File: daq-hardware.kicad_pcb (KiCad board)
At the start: 2 copper layers, 100 x 60 mm, 35 parts, among them J1 USB_B, J2 Micro_SD_Card_Det_Hirose_DM3AT, J3 Screw_Terminal_Thermo_1, J4 Screw_Terminal_Thermo_2, J5 Screw_Terminal_Thermo_3, J6 Screw_Terminal_Thermo_4, J7 Conn_01x02, J8 Screw_Terminal_01x02, Q1 MMDT2222A, U1 CP2102N-A01-GQFN24, U2 ESP32-WROOM-32D, U4 MAX31855RASA, U5 MAX31855RASA, U6 MAX31855RASA, U7 MAX31855RASA, U8 TPS62160DGK

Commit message: Layout for Pyros
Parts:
- added D3: FIRING, LED_SMD:LED_0805_2012Metric, F.Cu at (271.5, 80.0)
- added D4: DIODE, Diode_SMD:D_SMA, F.Cu at (272.8, 85.6)
- added J10: Screw_Terminal_01x02, TerminalBlock_Phoenix:TerminalBlock_Phoenix_MPT-0,5-2-2.54_1x02_P2.54mm_Horizontal, F.Cu at (280.9, 80.8)
- added J11: Screw_Terminal_01x02, TerminalBlock_Phoenix:TerminalBlock_Phoenix_MPT-0,5-2-2.54_1x02_P2.54mm_Horizontal, F.Cu at (280.9, 88.1)
- added JP1: SolderJumper_3_Open, Jumper:SolderJumper-3_P2.0mm_Open_TrianglePad1.0x1.5mm, F.Cu at (263.4, 75.2)
- added Q2: PMV20ENR, Package_TO_SOT_SMD:SOT-23, F.Cu at (267.2, 87.6)
- added R23: 1k, Resistor_SMD:R_0603_1608Metric, F.Cu at (273.8, 80.3)
- added R24: 500, Resistor_SMD:R_0603_1608Metric, F.Cu at (260.4, 87.6)
- added R25: 500, Resistor_SMD:R_0603_1608Metric, F.Cu at (263.1, 87.6)
- added U10: LTV-817S, Package_DIP:SMDIP-4_W9.53mm, F.Cu at (264.2, 82.0)
- renumbered C5 to C10, C6 to C11, C7 to C12, C8 to C13, C9 to C14, C10 to C15, C11 to C16, C14 to C6, C15 to C7, C4 to C9, J7 to J3, J8 to J4, J3 to J6, J4 to J7, J5 to J8, J6 to J9, R16 to R18, R17 to R19, R18 to R20, R3 to R4, R4 to R5, U8 to U4, U4 to U6, U5 to U7, U6 to U8, U7 to U9
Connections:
- J2 pad 10: (no net) -> Net-(J2-Pad10)
- J2 pad 9: (no net) -> Net-(J2-Pad9)
- U1 pad 1: (no net) -> Net-(U1-Pad1)
- U1 pad 10: (no net) -> Net-(U1-Pad10)
- U1 pad 11: (no net) -> Net-(U1-Pad11)
- U1 pad 12: (no net) -> Net-(U1-Pad12)
- U1 pad 13: (no net) -> Net-(U1-Pad13)
- U1 pad 14: (no net) -> Net-(U1-Pad14)
- U1 pad 15: (no net) -> Net-(U1-Pad15)
- U1 pad 16: (no net) -> Net-(U1-Pad16)
- U1 pad 17: (no net) -> Net-(U1-Pad17)
- U1 pad 18: (no net) -> Net-(U1-Pad18)
- U1 pad 19: (no net) -> Net-(U1-Pad19)
- U1 pad 22: (no net) -> Net-(U1-Pad22)
- U1 pad 23: (no net) -> Net-(U1-Pad23)
- U1 pad 24: (no net) -> Net-(U1-Pad24)
- U1 pad 8: (no net) -> Net-(R2-Pad2)
- U1 pad 9: (no net) -> Net-(U1-Pad9)
- U2 pad 17: (no net) -> Net-(U2-Pad17)
- U2 pad 18: (no net) -> Net-(U2-Pad18)
- U2 pad 19: (no net) -> Net-(U2-Pad19)
- U2 pad 20: (no net) -> Net-(U2-Pad20)
- U2 pad 21: (no net) -> Net-(U2-Pad21)
- U2 pad 22: (no net) -> Net-(U2-Pad22)
- U2 pad 27: (no net) -> Net-(U2-Pad27)
- U2 pad 28: (no net) -> Net-(U2-Pad28)
- U2 pad 29: (no net) -> /LED
- U2 pad 32: (no net) -> Net-(U2-Pad32)
- U2 pad 33: (no net) -> /SDA
- U2 pad 36: (no net) -> /SCL
- U2 pad 4: (no net) -> Net-(U2-Pad4)
- U2 pad 5: (no net) -> Net-(U2-Pad5)
- U2 pad 6: (no net) -> /PTAP1
- U2 pad 7: (no net) -> /PTAP3
- U2 pad 9: (no net) -> /PTAP2
- U4 pad 7: (no net) -> Net-(L1-Pad1)
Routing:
- net GND: track 0.00 -> 35.4 mm
- net Net-(D3-Pad2): track 0.00 -> 27.0 mm
- net Net-(J10-Pad1): track 0.00 -> 17.8 mm
- net Net-(D4-Pad2): track 0.00 -> 17.7 mm
- net Net-(D4-Pad1): track 0.00 -> 14.2 mm, vias 0 -> 1
- net Net-(R25-Pad1): track 0.00 -> 7.31 mm
- net +3V3: track 0.00 -> 6.53 mm
- net /pyro/CONT: track 0.00 -> 3.93 mm
- net Net-(D3-Pad1): track 0.00 -> 2.33 mm
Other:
- copper layers 2 -> 4
- net class Default: clearance 0.2 -> 0.127; trace_width 0.25 -> 0.2; via_dia 0.8 -> 0.6; via_drill 0.4 -> 0.35
- rule trace_clearance: 0.2 -> 0.127

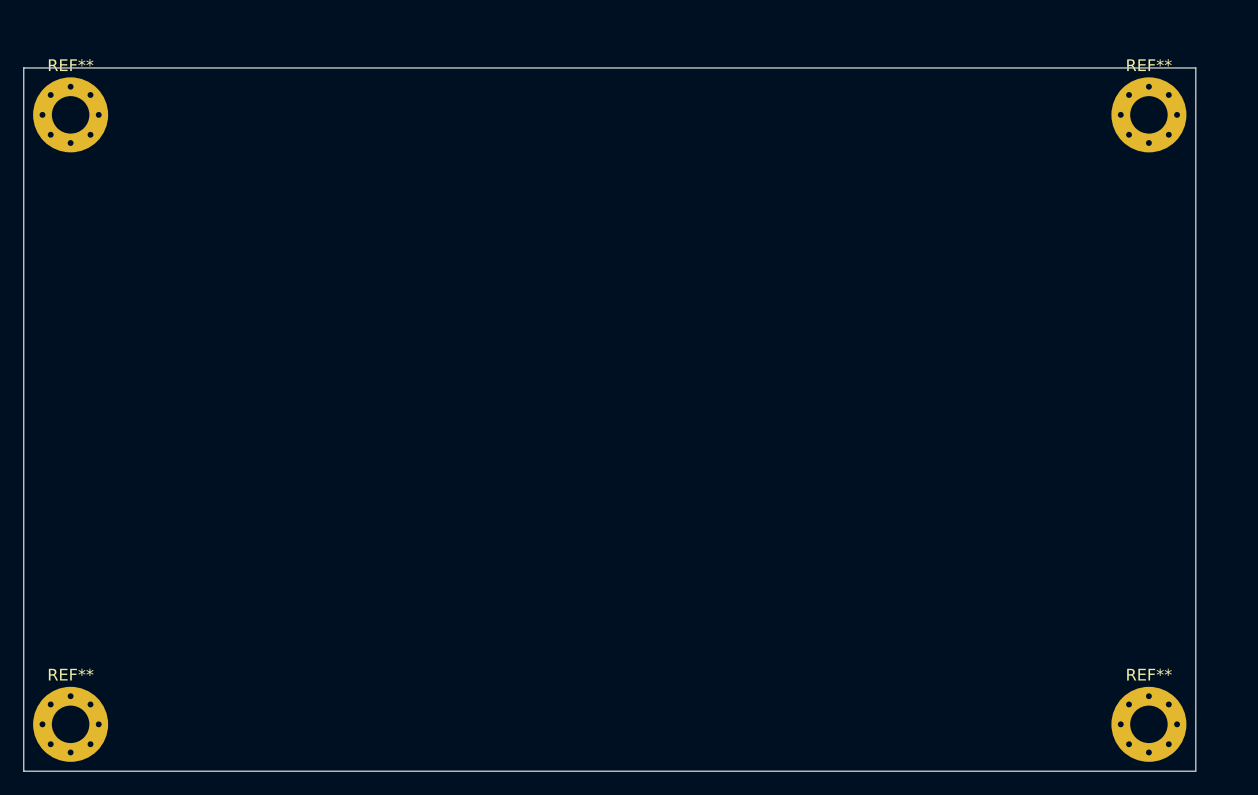
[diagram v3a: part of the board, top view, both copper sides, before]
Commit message: Via Shielding
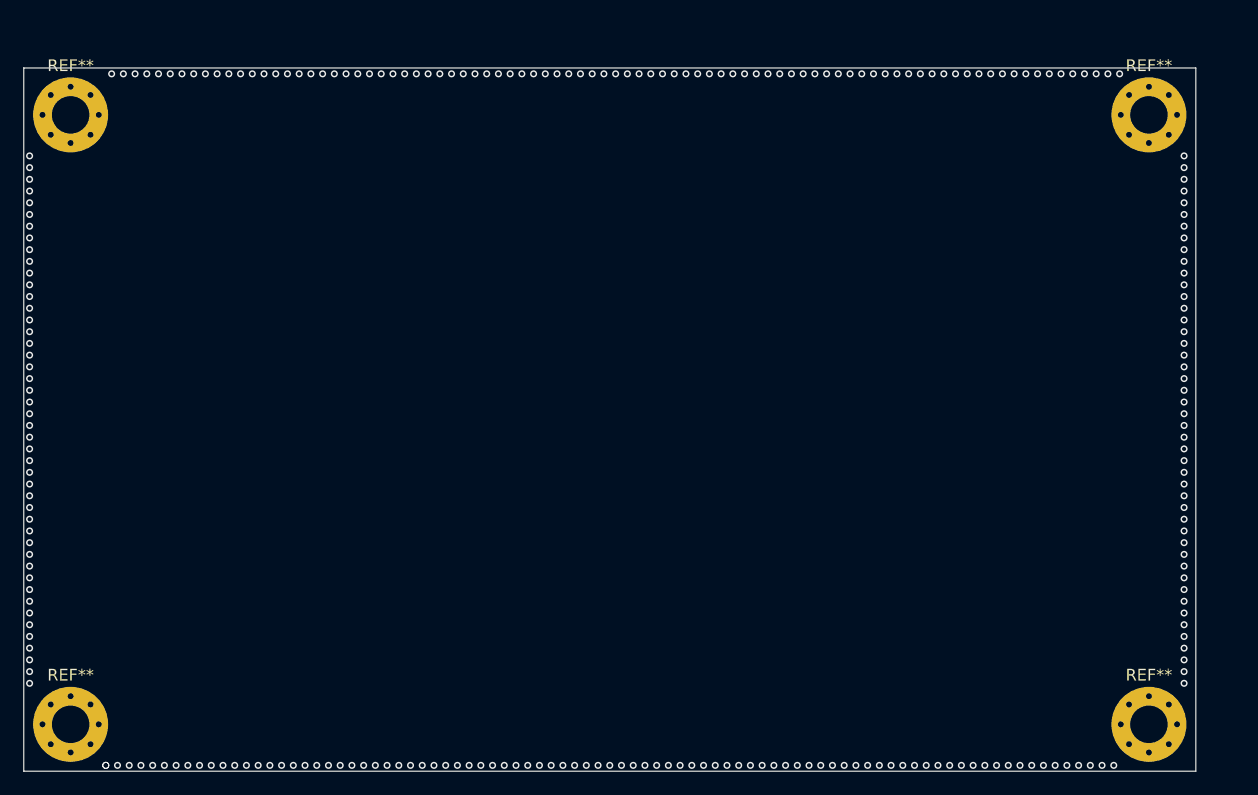
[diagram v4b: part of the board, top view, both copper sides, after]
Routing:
- net GND: vias 0 -> 266
- net (no net): vias 0 -> 1
- added copper zone on In1.Cu, net GND

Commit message: Not sure if this is gonna overwrite stuff but I try to push this anyway
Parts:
- moved JP1 105.1 mm to (169.4, 122.2)
- moved Q2 105.1 mm to (173.2, 134.6)
- moved R24 105.1 mm to (166.3, 134.6)
- moved U10 105.1 mm to (170.2, 129.0)
- moved D3 105.1 mm to (177.5, 127.0)
- moved D4 105.1 mm to (178.8, 132.6)
- moved R23 105.1 mm to (179.8, 127.3)
- moved R25 105.1 mm to (169.1, 134.6)
- moved J10 105.1 mm to (186.9, 127.8)
- moved J11 105.1 mm to (186.9, 135.1)
- moved C9 99.9 mm to (182.2, 91.5), turned to 180 degrees
- moved U9 96.9 mm to (180.0, 95.4), turned to 180 degrees
- moved U2 94.7 mm to (110.0, 120.5)
- moved C16 93.9 mm to (186.0, 94.2), turned to 270 degrees
- moved C15 90.3 mm to (182.2, 99.5), turned to 180 degrees
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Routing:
- net /SCLK: track 0.00 -> 96.6 mm
- net /MISO: track 0.00 -> 93.2 mm, vias 0 -> 2
- net /~TC_CS4: track 0.00 -> 87.1 mm, vias 0 -> 2
- net /~TC_CS2: track 0.00 -> 78.4 mm, vias 0 -> 2
- net /~TC_CS1: track 0.00 -> 73.7 mm, vias 0 -> 2
- net /~TC_CS3: track 0.00 -> 72.6 mm
- net VDD: track 0.00 -> 58.1 mm, vias 0 -> 2
- net GND: track 35.4 -> 75.4 mm, vias 266 -> 283
- net /SD_CLK: track 0.00 -> 36.9 mm, vias 0 -> 1
- net /SD_D1: track 0.00 -> 35.7 mm, vias 0 -> 1
- net +3V3: track 6.53 -> 40.3 mm, vias 0 -> 10
- net /RESET: track 0.00 -> 33.2 mm, vias 0 -> 2
- net /SD_D0: track 0.00 -> 26.0 mm, vias 0 -> 1
- net Net-(J1-Pad3): track 0.00 -> 23.6 mm
- net /SD_CMD: track 0.00 -> 21.1 mm, vias 0 -> 1
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
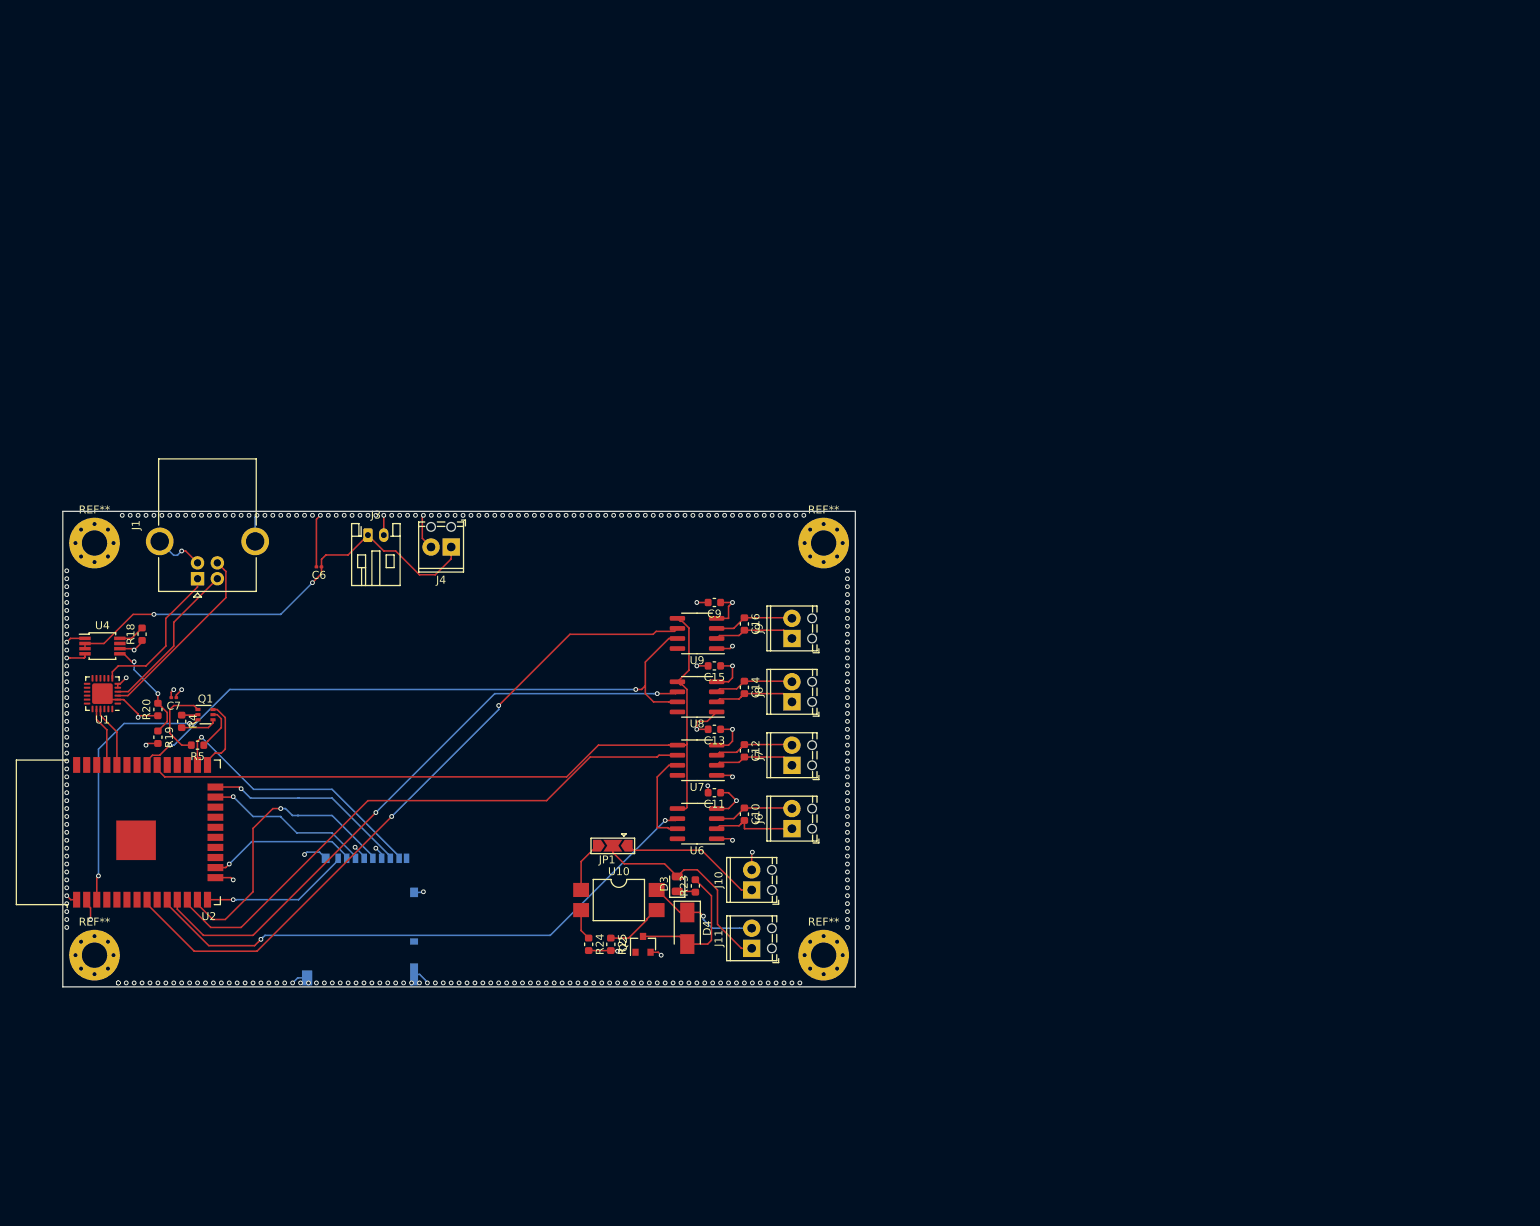
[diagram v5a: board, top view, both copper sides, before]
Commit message: Fixed conflicts, assigned all footprints.
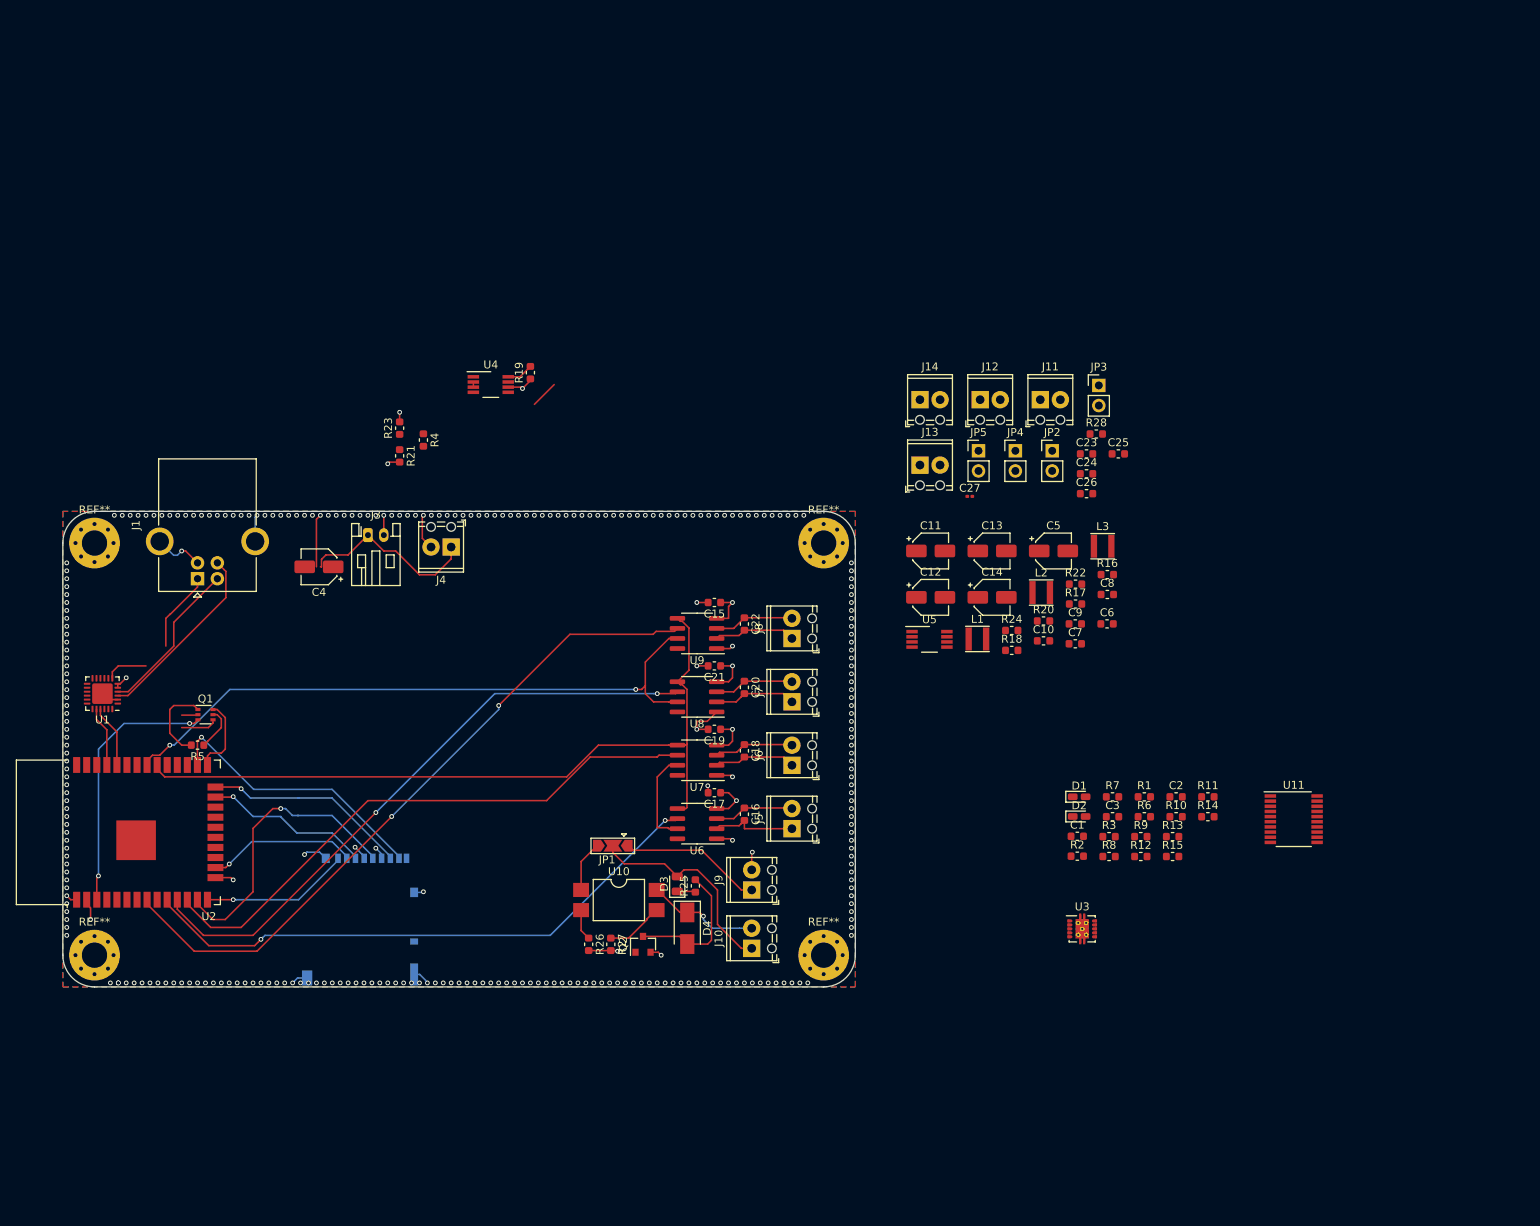
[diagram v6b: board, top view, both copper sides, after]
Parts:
- added C1: 100n, Capacitor_SMD:C_0603_1608Metric, F.Cu at (228.0, 121.0)
- added C10: 100n, Capacitor_SMD:C_0603_1608Metric, F.Cu at (223.7, 96.3)
- added C11: 10u, Capacitor_SMD:CP_Elec_4x5.4, F.Cu at (209.5, 85.0)
- added C12: 10u, Capacitor_SMD:CP_Elec_4x5.4, F.Cu at (209.5, 90.8)
- added C13: 10u, Capacitor_SMD:CP_Elec_4x5.4, F.Cu at (217.2, 85.0)
- added C14: 10u, Capacitor_SMD:CP_Elec_4x5.4, F.Cu at (217.2, 90.8)
- added C2: 1nF, Capacitor_SMD:C_0603_1608Metric, F.Cu at (240.5, 116.0)
- added C23: 10nF, Capacitor_SMD:C_0603_1608Metric, F.Cu at (229.2, 72.8)
- added C24: 10nF, Capacitor_SMD:C_0603_1608Metric, F.Cu at (229.2, 75.3)
- added C25: 10nF, Capacitor_SMD:C_0603_1608Metric, F.Cu at (233.2, 72.8)
- added C26: 10nF, Capacitor_SMD:C_0603_1608Metric, F.Cu at (229.2, 77.8)
- added C27: 220nF, Capacitor_SMD:C_0201_0603Metric, F.Cu at (214.4, 78.1)
- added C3: 1nF, Capacitor_SMD:C_0603_1608Metric, F.Cu at (232.4, 118.5)
- added C5: 10u, Capacitor_SMD:CP_Elec_4x5.4, F.Cu at (225.0, 85.0)
- added C6: 4u7, Capacitor_SMD:C_0603_1608Metric, F.Cu at (231.8, 94.2)
- added C8: 1u, Capacitor_SMD:C_0603_1608Metric, F.Cu at (231.8, 90.5)
- added C9: 1u, Capacitor_SMD:C_0603_1608Metric, F.Cu at (227.8, 94.2)
- added D1: LED, Diode_SMD:D_0603_1608Metric_Castellated, F.Cu at (228.2, 116.0)
- added D2: LED, Diode_SMD:D_0603_1608Metric_Castellated, F.Cu at (228.2, 118.5)
- added J11: Screw_Terminal_01x01, TerminalBlock_Phoenix:TerminalBlock_Phoenix_MPT-0,5-2-2.54_1x02_P2.54mm_Horizontal, F.Cu at (223.3, 65.9)
- added J12: Screw_Terminal_01x01, TerminalBlock_Phoenix:TerminalBlock_Phoenix_MPT-0,5-2-2.54_1x02_P2.54mm_Horizontal, F.Cu at (215.7, 65.9)
- added J13: Screw_Terminal_01x01, TerminalBlock_Phoenix:TerminalBlock_Phoenix_MPT-0,5-2-2.54_1x02_P2.54mm_Horizontal, F.Cu at (208.2, 74.2)
- added J14: Screw_Terminal_01x01, TerminalBlock_Phoenix:TerminalBlock_Phoenix_MPT-0,5-2-2.54_1x02_P2.54mm_Horizontal, F.Cu at (208.2, 65.9)
- added JP2: Jumper, Connector_PinHeader_2.54mm:PinHeader_1x02_P2.54mm_Vertical, F.Cu at (224.8, 72.4)
- added JP3: Jumper, Connector_PinHeader_2.54mm:PinHeader_1x02_P2.54mm_Vertical, F.Cu at (230.7, 64.1)
- added JP4: Jumper, Connector_PinHeader_2.54mm:PinHeader_1x02_P2.54mm_Vertical, F.Cu at (220.2, 72.4)
- added JP5: Jumper, Connector_PinHeader_2.54mm:PinHeader_1x02_P2.54mm_Vertical, F.Cu at (215.5, 72.4)
- added L1: 10u, Inductor_SMD:L_Taiyo-Yuden_NR-30xx, F.Cu at (215.4, 96.1)
- added L2: 2u2, Inductor_SMD:L_Taiyo-Yuden_NR-30xx, F.Cu at (223.4, 90.2)
- added L3: 2u2, Inductor_SMD:L_Taiyo-Yuden_NR-30xx, F.Cu at (231.2, 84.4)
- added R1: 10k, Resistor_SMD:R_0603_1608Metric, F.Cu at (236.5, 116.0)
- added R10: 470, Resistor_SMD:R_0603_1608Metric, F.Cu at (240.5, 118.5)
- added R11: 10k, Resistor_SMD:R_0603_1608Metric, F.Cu at (244.5, 116.0)
- added R12: 10k, Resistor_SMD:R_0603_1608Metric, F.Cu at (236.0, 123.5)
- added R13: 10k, Resistor_SMD:R_0603_1608Metric, F.Cu at (240.0, 121.0)
- added R14: 10k, Resistor_SMD:R_0603_1608Metric, F.Cu at (244.5, 118.5)
- added R15: 10k, Resistor_SMD:R_0603_1608Metric, F.Cu at (240.0, 123.5)
- added R16: 230k, Resistor_SMD:R_0603_1608Metric, F.Cu at (231.8, 88.0)
- added R17: 10k, Resistor_SMD:R_0603_1608Metric, F.Cu at (227.8, 91.7)
- added R18: 200k, Resistor_SMD:R_0603_1608Metric, F.Cu at (219.7, 97.5)
- added R2: 22k1, Resistor_SMD:R_0603_1608Metric, F.Cu at (228.0, 123.5)
- added R20: 100k, Resistor_SMD:R_0603_1608Metric, F.Cu at (223.7, 93.8)
- added R22: 52k5, Resistor_SMD:R_0603_1608Metric, F.Cu at (227.8, 89.2)
- added R24: 10k, Resistor_SMD:R_0603_1608Metric, F.Cu at (219.7, 95.0)
- added R28: 10k, Resistor_SMD:R_0603_1608Metric, F.Cu at (230.4, 70.2)
- added R3: 47k5, Resistor_SMD:R_0603_1608Metric, F.Cu at (232.0, 121.0)
- added R6: 10k, Resistor_SMD:R_0603_1608Metric, F.Cu at (236.5, 118.5)
- added R7: 470, Resistor_SMD:R_0603_1608Metric, F.Cu at (232.4, 116.0)
- added R8: 470, Resistor_SMD:R_0603_1608Metric, F.Cu at (232.0, 123.5)
- added R9: 470, Resistor_SMD:R_0603_1608Metric, F.Cu at (236.0, 121.0)
- added U11: ADS131M04, Housings_SSOP:TSSOP-20_4.4x6.5mm_Pitch0.65mm, F.Cu at (255.3, 118.8)
- added U3: TPS61093, Housings_SON:Texas_S-PWSON-N10_ThermalVias, F.Cu at (228.6, 132.7)
- added U5: TPS62160DGK, Housings_SSOP:VSSOP-8_3.0x3.0mm_Pitch0.65mm, F.Cu at (209.3, 96.2)
- C4: renamed from C6; footprint Capacitor_SMD:C_0201_0603Metric -> Capacitor_SMD:CP_Elec_4x5.4
- C7: value 22u -> 100n; footprint Capacitor_SMD:C_0201_0603Metric -> Capacitor_SMD:C_0603_1608Metric
- R21: renamed from R19; value 312k5 -> 62k5
- R23: renamed from R20; value 100k -> 20k
- U4: footprint Package_SO:MSOP-8_3x3mm_P0.65mm -> Housings_SSOP:VSSOP-8_3.0x3.0mm_Pitch0.65mm
- moved C7 114.0 mm to (227.8, 96.7), turned to 0 degrees
- moved R19 59.1 mm to (159.0, 62.5)
- moved U4 59.1 mm to (154.0, 64.0)
- moved R21 46.8 mm to (142.5, 73.0)
- moved R23 46.8 mm to (142.5, 69.5)
- moved R4 46.8 mm to (145.5, 71.0)
- renumbered C9 to C15, C10 to C16, C11 to C17, C12 to C18, C13 to C19, C14 to C20, C15 to C21, C16 to C22, J11 to J10, J6 to J5, J7 to J6, J8 to J7, J9 to J8, J10 to J9, R18 to R19, R23 to R25, R24 to R26, R25 to R27
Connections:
- net Net-(J1-Pad1) renamed VBUS
- C7 pad 1: +3V3 -> Net-(C7-Pad1)
- C7 pad 2: GND -> Net-(C7-Pad2)
- J2 pad 10: Net-(J2-Pad10) -> (no net)
- J2 pad 9: Net-(J2-Pad9) -> (no net)
- Q2 pad 1: /pyro/Fire -> /PYRO
- U1 pad 1: Net-(U1-Pad1) -> (no net)
- U1 pad 10: Net-(U1-Pad10) -> (no net)
- U1 pad 11: Net-(U1-Pad11) -> (no net)
- U1 pad 12: Net-(U1-Pad12) -> (no net)
- U1 pad 13: Net-(U1-Pad13) -> (no net)
- U1 pad 14: Net-(U1-Pad14) -> (no net)
- U1 pad 15: Net-(U1-Pad15) -> (no net)
- U1 pad 16: Net-(U1-Pad16) -> (no net)
- U1 pad 17: Net-(U1-Pad17) -> (no net)
- U1 pad 18: Net-(U1-Pad18) -> (no net)
- U1 pad 19: Net-(U1-Pad19) -> /RTS
- U1 pad 22: Net-(U1-Pad22) -> (no net)
- U1 pad 23: Net-(U1-Pad23) -> /DTR
- U1 pad 24: Net-(U1-Pad24) -> (no net)
- U1 pad 9: Net-(U1-Pad9) -> (no net)
- U2 pad 17: Net-(U2-Pad17) -> (no net)
- U2 pad 18: Net-(U2-Pad18) -> (no net)
- U2 pad 19: Net-(U2-Pad19) -> (no net)
- U2 pad 20: Net-(U2-Pad20) -> (no net)
- U2 pad 21: Net-(U2-Pad21) -> (no net)
- U2 pad 22: Net-(U2-Pad22) -> (no net)
- U2 pad 27: Net-(U2-Pad27) -> (no net)
- U2 pad 28: Net-(U2-Pad28) -> /CLKOUT
- U2 pad 32: Net-(U2-Pad32) -> (no net)
- U2 pad 33: /SDA -> /PYRO
- U2 pad 36: /SCL -> (no net)
- U2 pad 4: Net-(U2-Pad4) -> (no net)
- U2 pad 5: Net-(U2-Pad5) -> (no net)
- U2 pad 6: /PTAP1 -> (no net)
- U2 pad 7: /PTAP3 -> (no net)
- U2 pad 9: /PTAP2 -> (no net)
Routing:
- net VDD: track 58.1 -> 23.8 mm, vias 2 -> 0
- net Net-(J9-Pad1): track 17.8 -> 0.00 mm
- net Net-(J10-Pad1): track 0.00 -> 17.8 mm
- net GND: track 75.4 -> 62.7 mm, vias 283 -> 289
- net Net-(R21-Pad1): track 13.2 -> 1.21 mm, vias 2 -> 1
- net +3V3: track 40.3 -> 39.0 mm, vias 10 -> 9
- net (no net): vias 1 -> 0
- added copper zone on In2.Cu, net +3V3
- added copper zone on B.Cu, net GND
- added copper zone on F.Cu, net GND
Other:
- outline, holes or cut-outs redrawn
